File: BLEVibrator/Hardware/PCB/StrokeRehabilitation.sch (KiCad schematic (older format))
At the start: 26 parts, among them CON1 USB-MICRO-B, P2 Programming Header, Q1 MOS_P, Q2 MOSFET_N, SW1 SWITCH_INV, U1 MCP73833, U2 TPS73701_DRV_6, U3 RFD22301, U4 Brushed_DC_motor

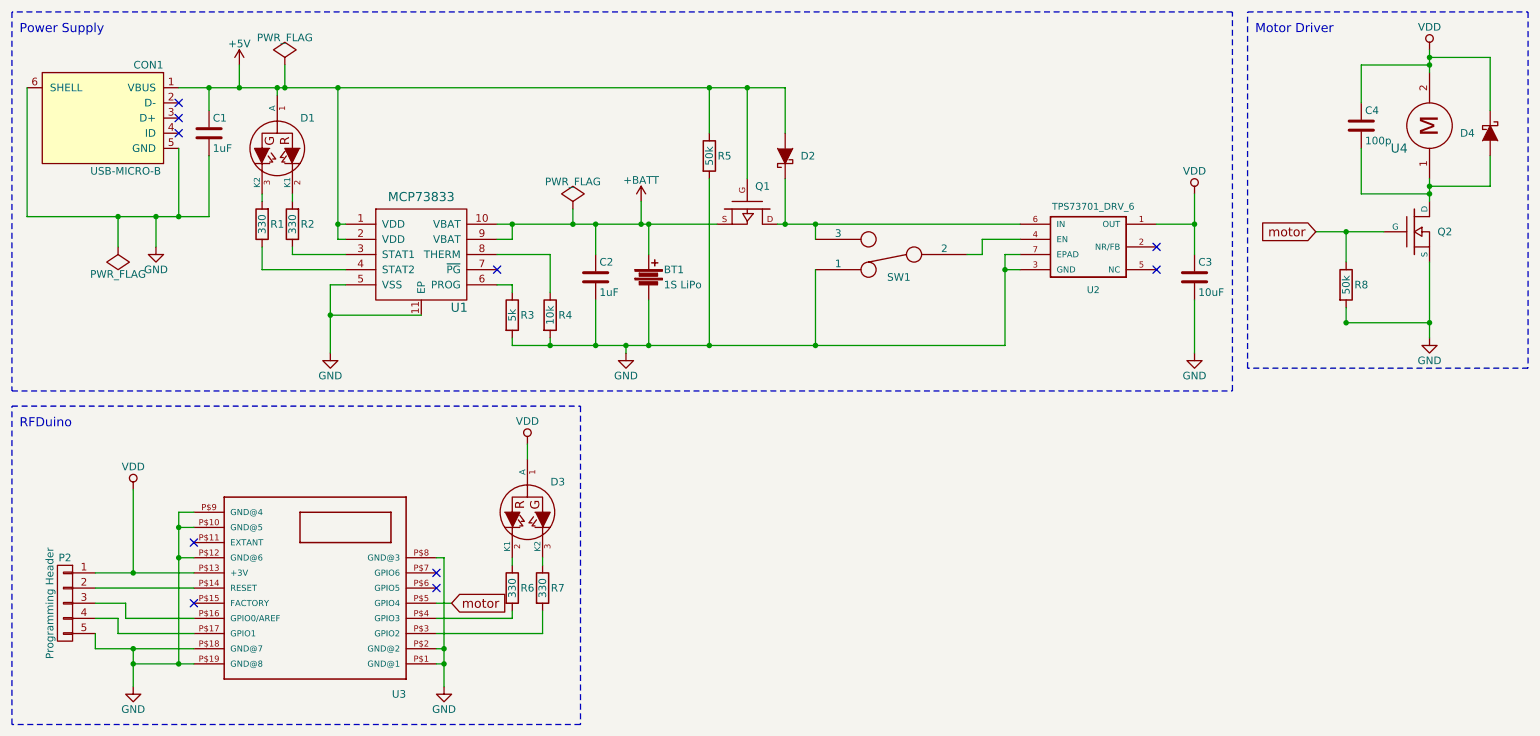
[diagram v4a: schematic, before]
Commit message: Added circuitry to enable monitoring of the LiPo voltage. Based on https://devzone.nordicsemi.com/question/990/how-to-measure-lithium-battery-voltage/ and https://devzone.nordicsemi.com/blogs/30/measuring-lithium-battery-voltage-with-voltage-div/
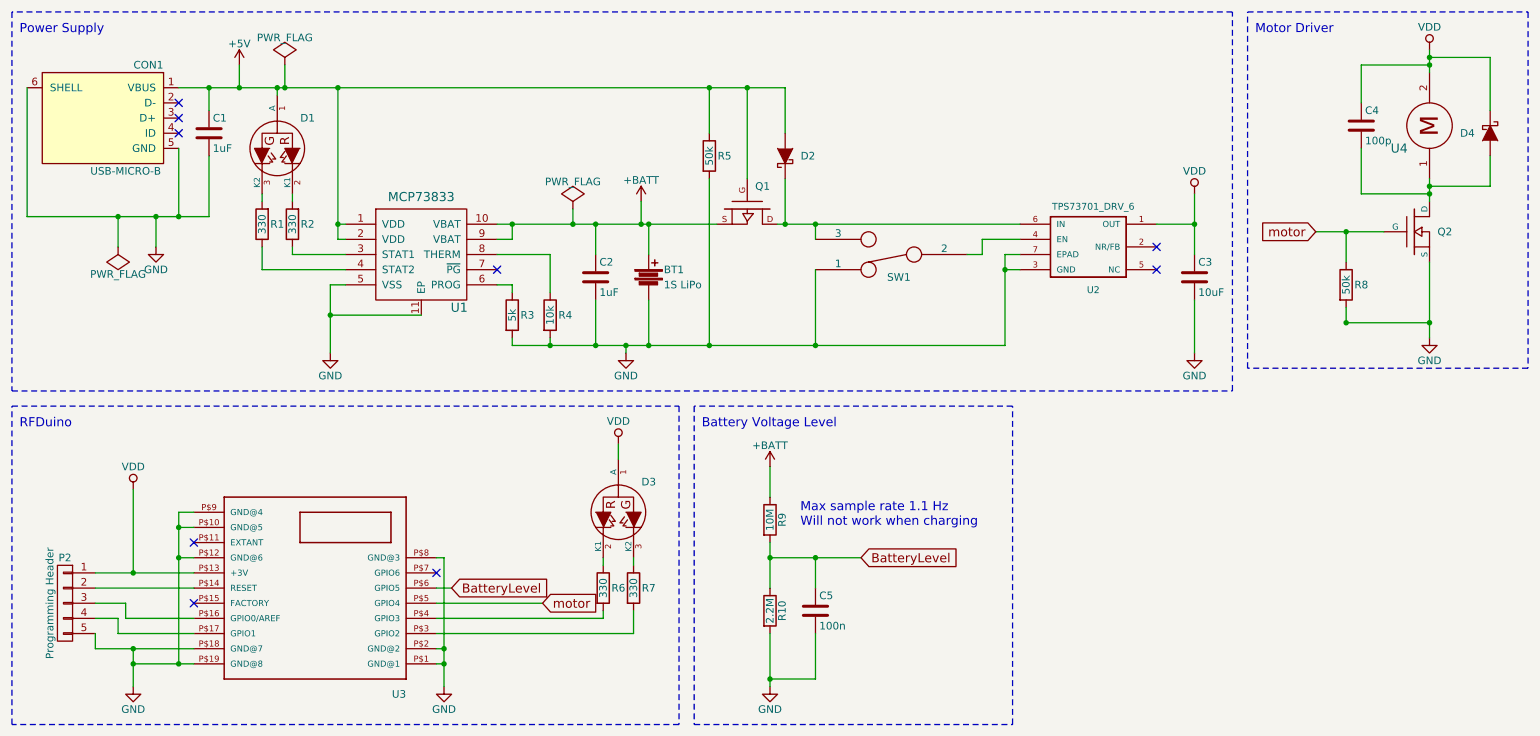
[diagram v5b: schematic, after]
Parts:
- added C5: 100n, symbol C
- added R10: 2.2M, symbol R
- added R9: 10M, symbol R
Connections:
- net +BATT: now also R9.1
- net GND: now also C5.2, R10.2
- net BatteryLevel: now reaches U3.P$6 (GPIO5)
- net BatteryLevel: now also C5.1, R10.1, R9.2
- no-connect marks 10 -> 9
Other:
- note added: "Battery Voltage Level"
- note added: "Max sample rate 1.1 Hz\nWill not work when charging"
- moved on the sheet: D3, R6, R7

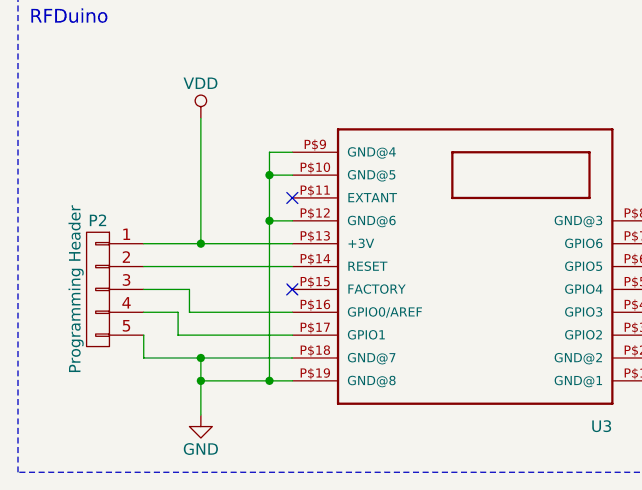
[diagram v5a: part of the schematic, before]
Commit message: Adding a test point for FACTORY pin of the RFDuino, in case SWD programming is needed in the future
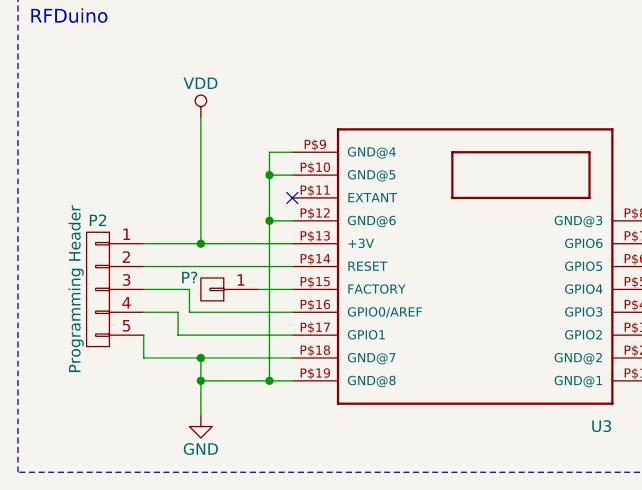
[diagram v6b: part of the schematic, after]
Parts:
- added P?: CONN_01X01, symbol CONN_01X01
- C5: footprint (none) -> Capacitors_SMD:C_0603
- R10, R9: footprint (none) -> Resistors_SMD:R_0603
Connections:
- net at U3.P$15 (FACTORY): now also P?.1 (P1)
- no-connect marks 9 -> 8
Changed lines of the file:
@@
 $EndComp
 $Comp
-L VDD #PWR14
+L VDD #PWR01
 U 1 1 56C747A7
 P 9950 850
-F 0 "#PWR14" H 9950 700 50  0001 C CNN
+F 0 "#PWR01" H 9950 700 50  0001 C CNN
 F 1 "VDD" H 9950 1000 50  0000 C CNN
 F 2 "" H 9950 850 50  0000 C CNN
@@
 $EndComp
 $Comp
-L GND #PWR15
+L GND #PWR02
 U 1 1 56C747A8
 P 9950 2750
-F 0 "#PWR15" H 9950 2500 50  0001 C CNN
+F 0 "#PWR02" H 9950 2500 50  0001 C CNN
 F 1 "GND" H 9950 2600 50  0000 C CNN
 F 2 "" H 9950 2750 50  0000 C CNN
@@
 $EndComp
 $Comp
-L PWR_FLAG #FLG1
+L PWR_FLAG #FLG03
 U 1 1 56C747AA
 P 1300 2150
-F 0 "#FLG1" H 1300 2245 50  0001 C CNN
+F 0 "#FLG03" H 1300 2245 50  0001 C CNN
 F 1 "PWR_FLAG" H 1300 2330 50  0000 C CNN
 F 2 "" H 1300 2150 50  0000 C CNN
@@
 $EndComp
 $Comp
-L VDD #PWR12
+L VDD #PWR04
 U 1 1 56C758CB
 P 8400 1800
-F 0 "#PWR12" H 8400 1650 50  0001 C CNN
+F 0 "#PWR04" H 8400 1650 50  0001 C CNN
 F 1 "VDD" H 8400 1950 50  0000 C CNN
 F 2 "" H 8400 1800 50  0000 C CNN
@@
 $EndComp
 $Comp
-L GND #PWR13
+L GND #PWR05
 U 1 1 56C759DE
 P 8400 2850
-F 0 "#PWR13" H 8400 2600 50  0001 C CNN
+F 0 "#PWR05" H 8400 2600 50  0001 C CNN
 F 1 "GND" H 8400 2700 50  0000 C CNN
 F 2 "" H 8400 2850 50  0000 C CNN
@@
 $EndComp
 $Comp
-L VDD #PWR1
+L VDD #PWR06
 U 1 1 56CB1B18
 P 1400 3750
-F 0 "#PWR1" H 1400 3600 50  0001 C CNN
+F 0 "#PWR06" H 1400 3600 50  0001 C CNN
 F 1 "VDD" H 1400 3900 50  0000 C CNN
 F 2 "" H 1400 3750 50  0000 C CNN
@@
 $EndComp
 $Comp
-L GND #PWR2
+L GND #PWR07
 U 1 1 56CB200B
 P 1400 5050
-F 0 "#PWR2" H 1400 4800 50  0001 C CNN
+F 0 "#PWR07" H 1400 4800 50  0001 C CNN
 F 1 "GND" H 1400 4900 50  0000 C CNN
 F 2 "" H 1400 5050 50  0000 C CNN
@@
 $EndComp
 NoConn ~ 1800 4100
-NoConn ~ 1800 4500
-$Comp
-L GND #PWR6
+$Comp
+L GND #PWR08
 U 1 1 56CB2639
 P 3450 5050
-F 0 "#PWR6" H 3450 4800 50  0001 C CNN
+F 0 "#PWR08" H 3450 4800 50  0001 C CNN
 F 1 "GND" H 3450 4900 50  0000 C CNN
 F 2 "" H 3450 5050 50  0000 C CNN
@@
 $EndComp
 $Comp
-L VDD #PWR7
+L VDD #PWR09
 U 1 1 56CB3133
 P 4600 3450
-F 0 "#PWR7" H 4600 3300 50  0001 C CNN
+F 0 "#PWR09" H 4600 3300 50  0001 C CNN
 F 1 "VDD" H 4600 3600 50  0000 C CNN
 F 2 "" H 4600 3450 50  0000 C CNN
@@
 $EndComp
 $Comp
-L GND #PWR3
+L GND #PWR010
 U 1 1 575981D1
 P 1550 2150
-F 0 "#PWR3" H 1550 1900 50  0001 C CNN
+F 0 "#PWR010" H 1550 1900 50  0001 C CNN
 F 1 "GND" H 1550 2000 50  0000 C CNN
 F 2 "" H 1550 2150 50  0000 C CNN
@@
 $EndComp
 $Comp
-L GND #PWR5
+L GND #PWR011
 U 1 1 575986DE
 P 2700 2850
-F 0 "#PWR5" H 2700 2600 50  0001 C CNN
+F 0 "#PWR011" H 2700 2600 50  0001 C CNN
 F 1 "GND" H 2700 2700 50  0000 C CNN
 F 2 "" H 2700 2850 50  0000 C CNN
@@
 $EndComp
 $Comp
-L +5V #PWR4
+L +5V #PWR012
 U 1 1 575992A8
 P 2100 950
-F 0 "#PWR4" H 2100 800 50  0001 C CNN
+F 0 "#PWR012" H 2100 800 50  0001 C CNN
 F 1 "+5V" H 2100 1090 50  0000 C CNN
 F 2 "" H 2100 950 50  0000 C CNN
@@
 $EndComp
 $Comp
-L PWR_FLAG #FLG2
+L PWR_FLAG #FLG013
 U 1 1 57599918
 P 2400 950
-F 0 "#FLG2" H 2400 1045 50  0001 C CNN
+F 0 "#FLG013" H 2400 1045 50  0001 C CNN
 F 1 "PWR_FLAG" H 2400 1130 50  0000 C CNN
 F 2 "" H 2400 950 50  0000 C CNN
@@
 $EndComp
 $Comp
-L GND #PWR8
+L GND #PWR014
 U 1 1 5759AB91
 P 4650 2850
-F 0 "#PWR8" H 4650 2600 50  0001 C CNN
+F 0 "#PWR014" H 4650 2600 50  0001 C CNN
 F 1 "GND" H 4650 2700 50  0000 C CNN
 F 2 "" H 4650 2850 50  0000 C CNN
@@
 $EndComp
 $Comp
-L +BATT #PWR9
+L +BATT #PWR015
 U 1 1 5759C5A4
 P 4750 1850
-F 0 "#PWR9" H 4750 1700 50  0001 C CNN
+F 0 "#PWR015" H 4750 1700 50  0001 C CNN
 F 1 "+BATT" H 4750 1990 50  0000 C CNN
 F 2 "" H 4750 1850 50  0000 C CNN
@@
 Connection ~ 2700 2600
 $Comp
-L PWR_FLAG #FLG3
+L PWR_FLAG #FLG016
 U 1 1 5768A320
 P 4300 1900
-F 0 "#FLG3" H 4300 1995 50  0001 C CNN
+F 0 "#FLG016" H 4300 1995 50  0001 C CNN
 F 1 "PWR_FLAG" H 4300 2080 50  0000 C CNN
 F 2 "" H 4300 1900 50  0000 C CNN
@@
 F 0 "R10" V 5680 4550 50  0000 C CNN
 F 1 "2.2M" V 5600 4550 50  0000 C CNN
-F 2 "" V 5530 4550 50  0000 C CNN
+F 2 "Resistors_SMD:R_0603" V 5530 4550 50  0001 C CNN
 F 3 "" H 5600 4550 50  0000 C CNN
 	1    5600 4550
@@
 F 0 "R9" V 5680 3950 50  0000 C CNN
 F 1 "10M" V 5600 3950 50  0000 C CNN
-F 2 "" V 5530 3950 50  0000 C CNN
+F 2 "Resistors_SMD:R_0603" V 5530 3950 50  0001 C CNN
 F 3 "" H 5600 3950 50  0000 C CNN
 	1    5600 3950
@@
 F 0 "C5" H 5925 4650 50  0000 L CNN
 F 1 "100n" H 5925 4450 50  0000 L CNN
-F 2 "" H 5938 4400 50  0000 C CNN
+F 2 "Capacitors_SMD:C_0603" H 5938 4400 50  0001 C CNN
 F 3 "" H 5900 4550 50  0000 C CNN
 	1    5900 4550
@@
 $EndComp
 $Comp
-L +BATT #PWR10
+L +BATT #PWR017
 U 1 1 576D613A
 P 5600 3600
-F 0 "#PWR10" H 5600 3450 50  0001 C CNN
+F 0 "#PWR017" H 5600 3450 50  0001 C CNN
 F 1 "+BATT" H 5600 3740 50  0000 C CNN
 F 2 "" H 5600 3600 50  0000 C CNN
@@
 	5600 4100 5600 4400
 $Comp
-L GND #PWR11
+L GND #PWR018
 U 1 1 576D6615
 P 5600 5050
-F 0 "#PWR11" H 5600 4800 50  0001 C CNN
+F 0 "#PWR018" H 5600 4800 50  0001 C CNN
 F 1 "GND" H 5600 4900 50  0000 C CNN
 F 2 "" H 5600 5050 50  0000 C CNN
@@
 Wire Notes Line
 	7200 3200 5100 3200
+$Comp
+L CONN_01X01 P?
+U 1 1 576D7C19
+P 1450 4500
+F 0 "P?" H 1550 4450 50  0000 C CNN
+F 1 "CONN_01X01" V 1550 4500 50  0001 C CNN
+F 2 "" H 1450 4500 50  0000 C CNN
+F 3 "" H 1450 4500 50  0000 C CNN
+	1    1450 4500
+	-1   0    0    1
+$EndComp
+Wire Wire Line
+	1650 4500 1800 4500
 $EndSCHEMATC
